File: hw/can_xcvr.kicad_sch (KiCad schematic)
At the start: 6 parts, among them U6 ATA6563-GAQW1

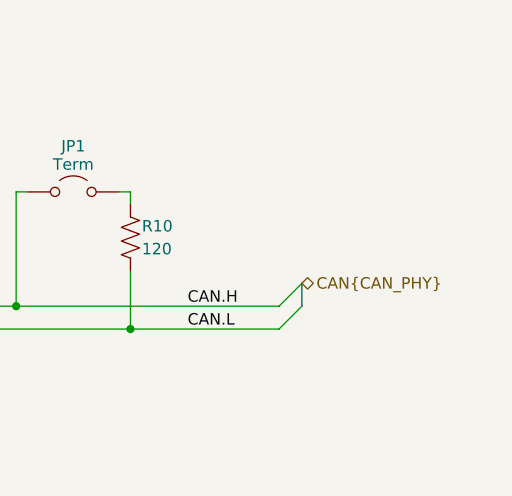
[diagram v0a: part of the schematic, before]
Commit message: hw: top level schematic
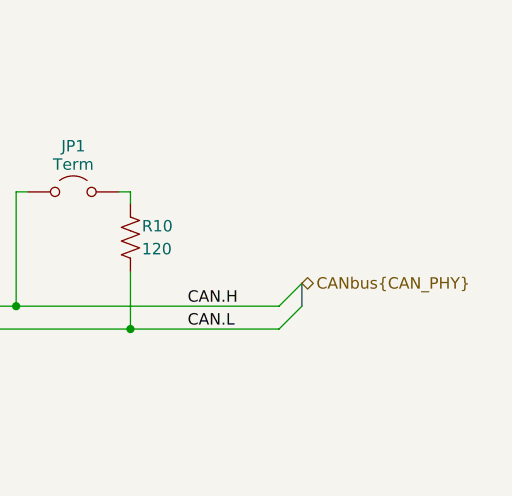
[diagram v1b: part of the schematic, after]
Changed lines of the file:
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@@
+		)
+	)
+	(hierarchical_label "CANbus{CAN_PHY}"
+		(shape bidirectional)
+		(at 139.7 55.88 0)
+		(effects
+			(font
+				(size 1.27 1.27)
+			)
+			(justify left)
 		)
 	)
@@
 		)
 	)
-	(hierarchical_label "CAN{CAN_PHY}"
-		(shape bidirectional)
-		(at 139.7 55.88 0)
-		(effects
-			(font
-				(size 1.27 1.27)
-			)
-			(justify left)
-		)
-	)

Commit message: hw: erc: can
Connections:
- net CAN.H renamed CAN1.H
- net CAN.L renamed CAN1.L
- net FDCAN1.RX renamed CAN1.RX
- net FDCAN1.TX renamed CAN1.TX
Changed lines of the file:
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@@
 		)
 	)
-	(label "CAN.L"
+	(label "CAN1.L"
 		(at 127 60.96 0)
 		(effects
@@
 		)
 	)
-	(label "FDCAN1.RX"
+	(label "CAN1.RX"
 		(at 58.42 63.5 180)
 		(effects
@@
 		)
 	)
-	(label "FDCAN1.TX"
+	(label "CAN1.TX"
 		(at 58.42 55.88 180)
 		(effects
@@
 		)
 	)
-	(label "CAN.H"
+	(label "CAN1.H"
 		(at 127 58.42 0)
 		(effects
@@
 		)
 	)
-	(hierarchical_label "CANbus{CAN_PHY}"
+	(hierarchical_label "CAN1{CAN_PHY}"
 		(shape bidirectional)
 		(at 139.7 55.88 0)
@@
 		)
 	)
-	(hierarchical_label "FDCAN1{CAN}"
+	(hierarchical_label "CAN1{CAN_IF}"
 		(shape bidirectional)
 		(at 38.1 53.34 180)
